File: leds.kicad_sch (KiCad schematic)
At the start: 193 parts

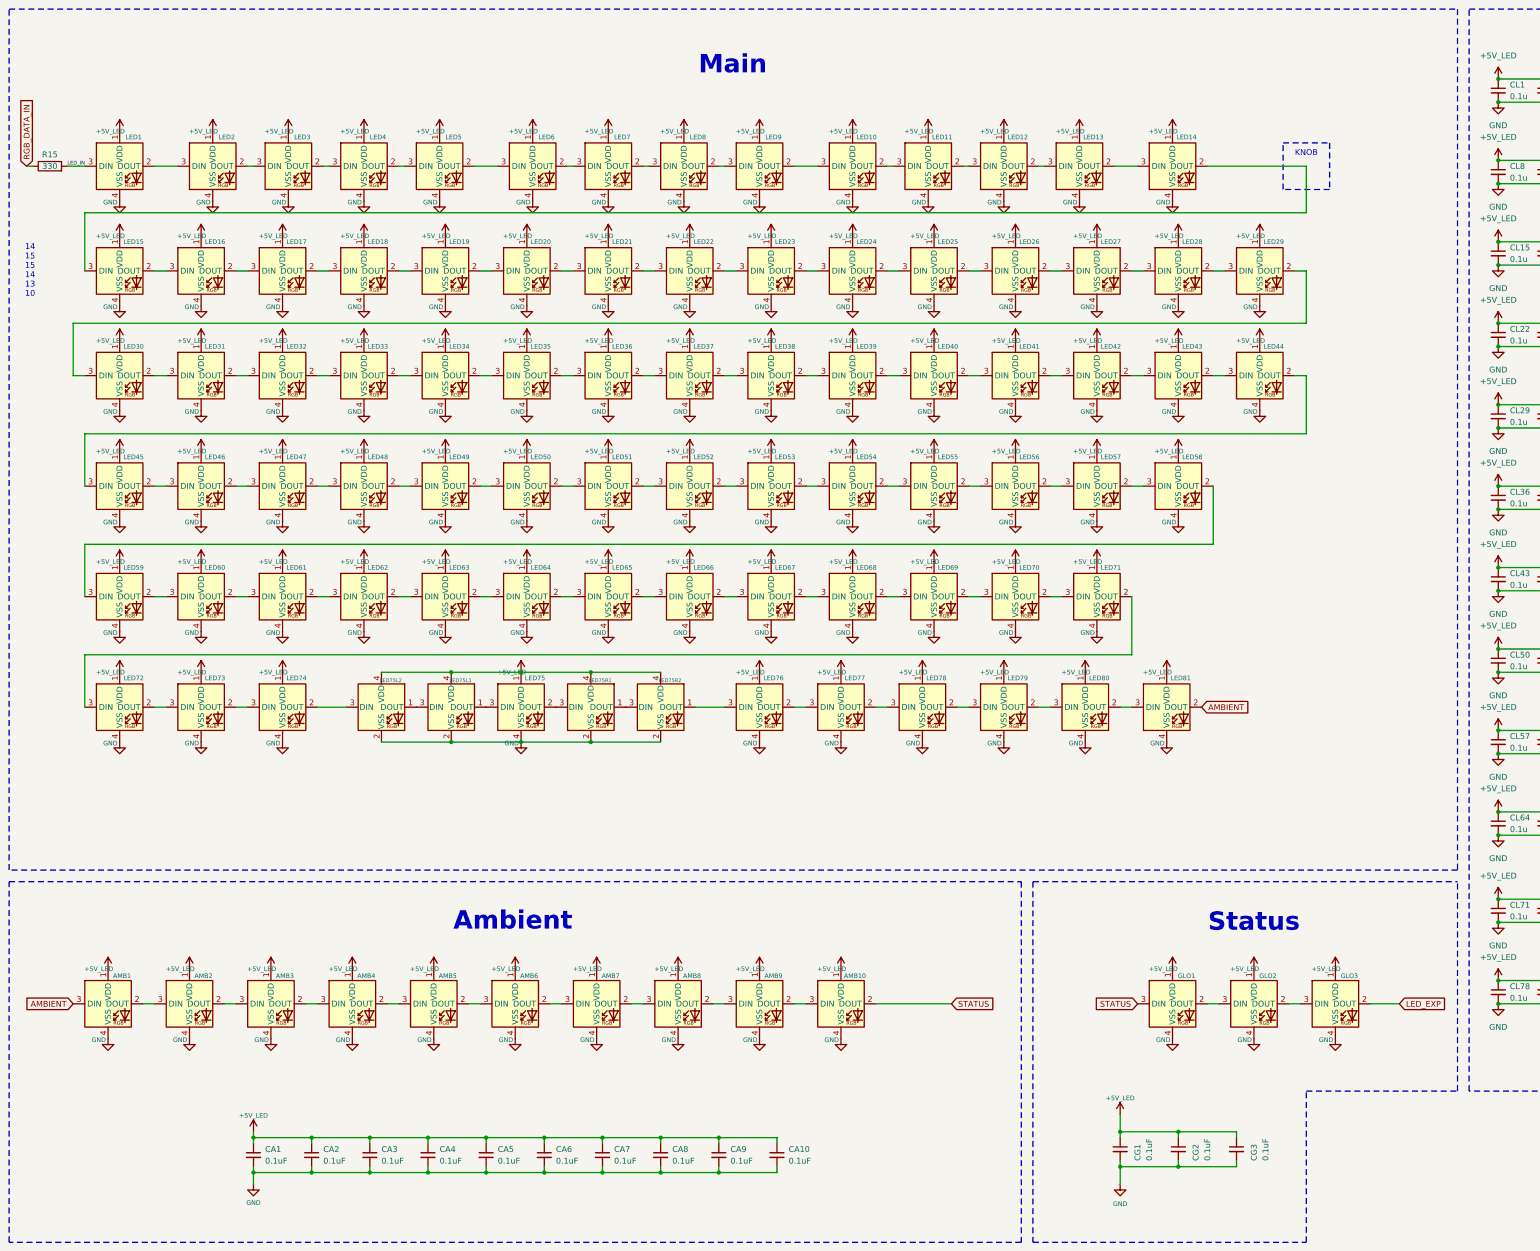
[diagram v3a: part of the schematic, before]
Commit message: PCB rev1 done — schematic/layout updates, drop stale production exports
- Schematic + PCB updates across VLT.kicad_pcb/sch, leds.kicad_sch, sensors.kicad_sch
- Remove production/ rev1 exports (zip/bom/positions/netlist) — regenerated on demand
- Drop fabrication-toolkit-options.json (not used)
- gitignore VLT+Dev/ experimental layouts
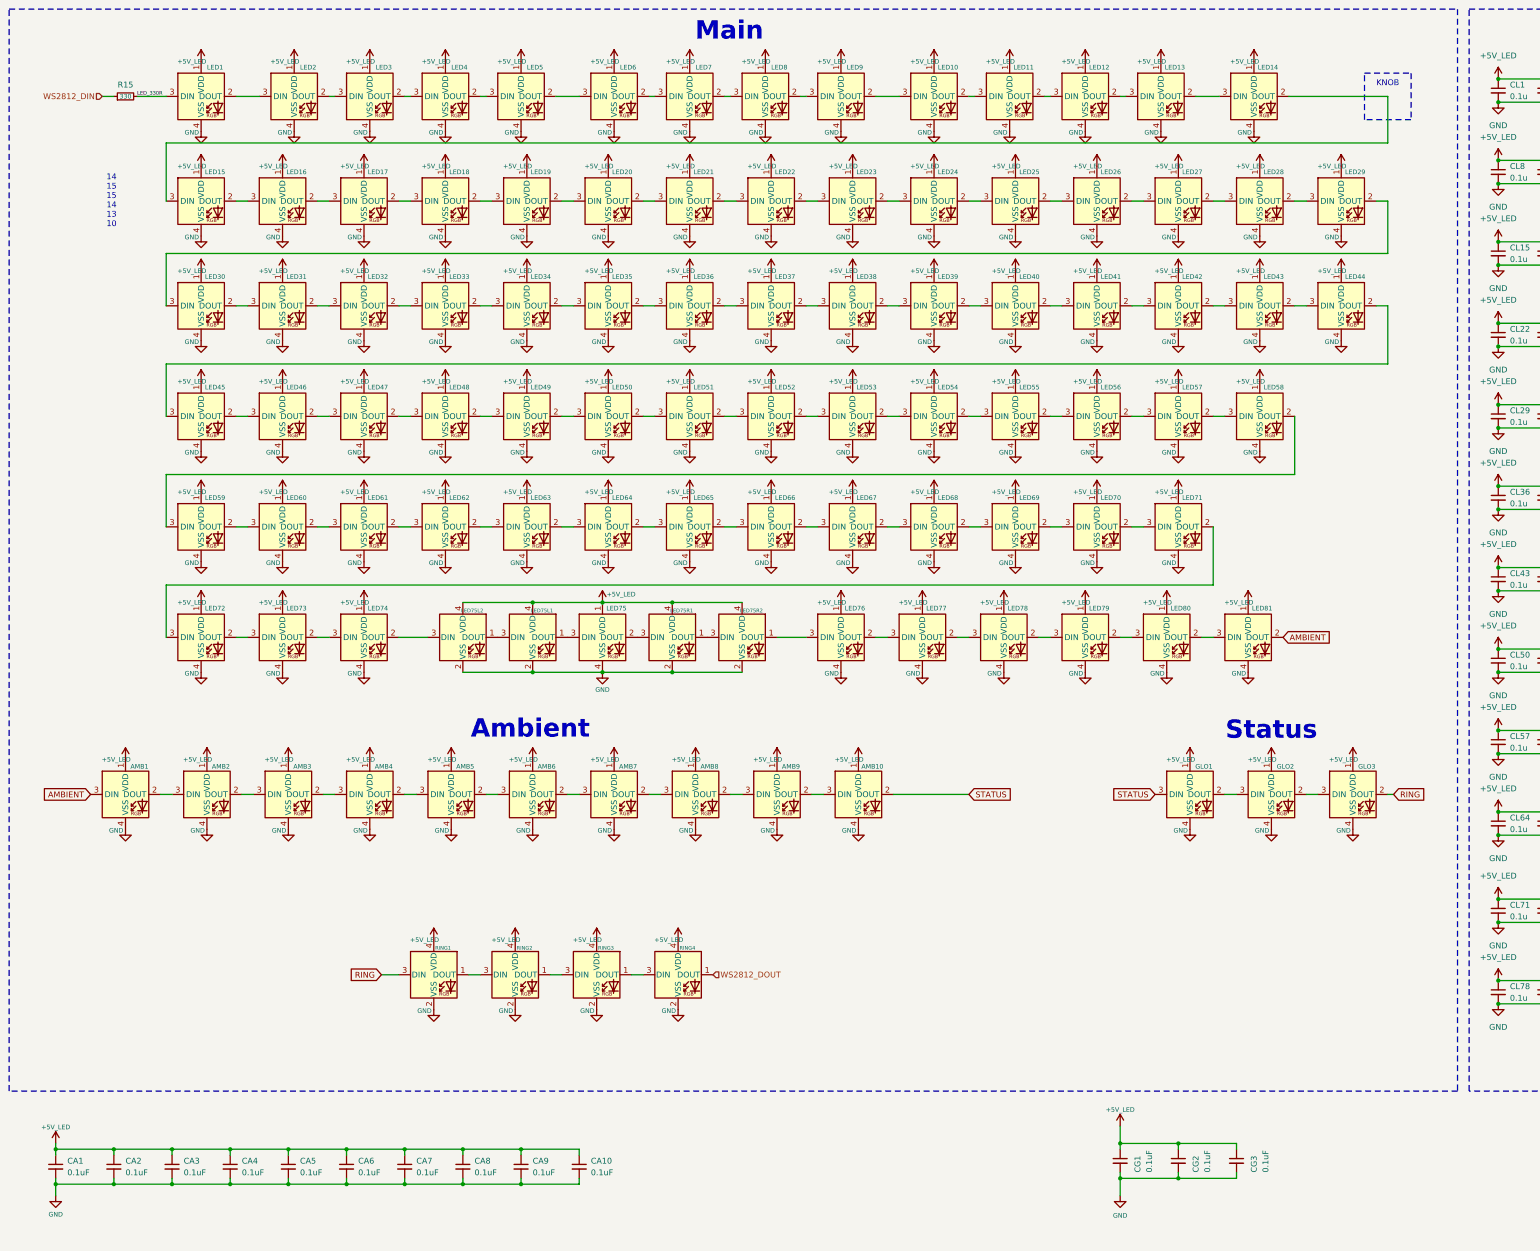
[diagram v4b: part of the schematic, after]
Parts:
- added RING1, RING2, RING3, RING4: WS2812_2020, sk6805-1515:sk68015-1515, symbol Mars_Library:SK6805-1515
- R15: symbol Device:R -> Mars_Library:Resistor_R_0603
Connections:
- net +5V_LED: now also RING1.4 (VDD), RING2.4 (VDD), RING3.4 (VDD), RING4.4 (VDD)
- net GND: now also RING1.2 (VSS), RING2.2 (VSS), RING3.2 (VSS), RING4.2 (VSS)
- net LED_EXP renamed RING
- net RING: now also RING1.3 (DIN)
- net LED_IN renamed LED_330R
- net RGB_DATA_IN renamed WS2812_DIN
- new net: RING1.1 (DOUT), RING2.3 (DIN)
- new net: RING3.1 (DOUT), RING4.3 (DIN)
- new net: RING2.1 (DOUT), RING3.3 (DIN)
- new net WS2812_DOUT: RING4.1 (DOUT)
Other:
- moved on the sheet: AMB1, AMB10, AMB2, AMB3, AMB4, AMB5, AMB6, AMB7, AMB8, AMB9, CA1, CA10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
